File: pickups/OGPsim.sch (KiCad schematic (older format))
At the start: 6 parts, among them Q3 QSB363, Q4 QSB363

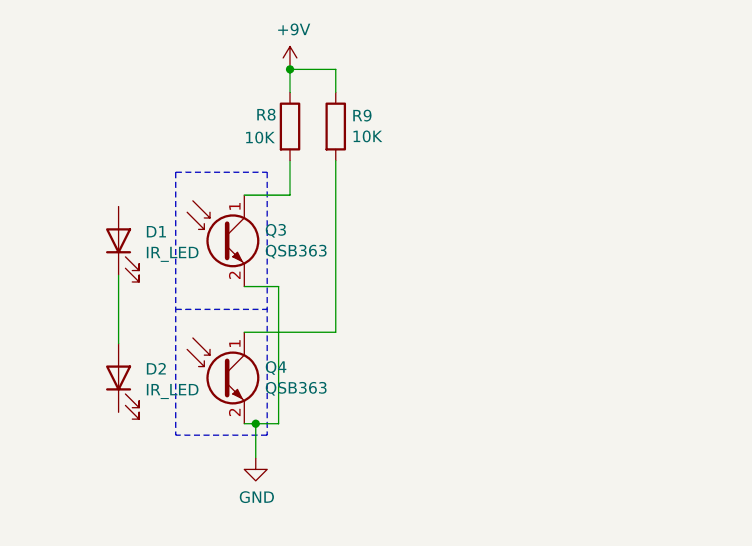
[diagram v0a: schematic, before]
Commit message: Added solder pads to pickup and adjusted placement of solder pads on demodulator.
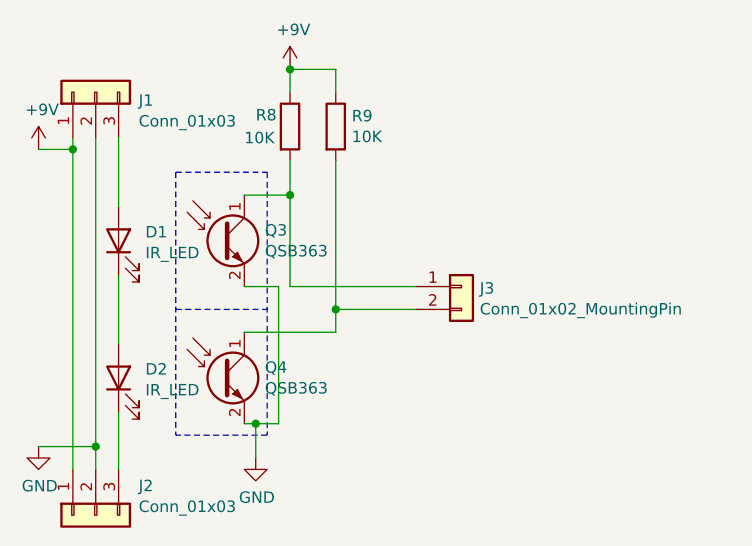
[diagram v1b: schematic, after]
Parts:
- added J1, J2: Conn_01x03, Connect:GS3, symbol Connector_Generic:Conn_01x03
- added J3: Conn_01x02_MountingPin, Connect:GS2, symbol Connector_Generic:Conn_01x02
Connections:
- net +9V: now also J1.1 (Pin_1), J2.1 (Pin_1)
- net GND: now also J1.2 (Pin_2), J2.2 (Pin_2)
- net at D1.2 (A): now also J1.3 (Pin_3)
- net at D2.1 (K): now also J2.3 (Pin_3)
- net at Q4.1 (C), R9.2: now also J3.2 (Pin_2)
- net at Q3.1 (C), R8.2: now also J3.1 (Pin_1)
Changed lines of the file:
@@
 	5150 4000 5550 4000
 Wire Wire Line
-	5850 3350 5850 4100
+	5850 3350 5850 4000
 $Comp
 L power:GND #PWR0102
@@
 Wire Wire Line
 	4900 3850 4900 4150
+$Comp
+L Connector_Generic:Conn_01x02 J3
+U 1 1 6127CF70
+P 6400 3900
+F 0 "J3" H 6480 3892 50  0000 L CNN
+F 1 "Conn_01x02_MountingPin" H 6480 3801 50  0000 L CNN
+F 2 "Connect:GS2" H 6400 3900 50  0001 C CNN
+F 3 "~" H 6400 3900 50  0001 C CNN
+	1    6400 3900
+	1    0    0    -1
+$EndComp
+Wire Wire Line
+	5850 4000 6200 4000
+Connection ~ 5850 4000
+Wire Wire Line
+	5850 4000 5850 4100
+Wire Wire Line
+	5650 3500 5650 3900
+Wire Wire Line
+	5650 3900 6200 3900
+Connection ~ 5650 3500
+$Comp
+L Connector_Generic:Conn_01x03 J1
+U 1 1 6127E563
+P 4800 3050
+F 0 "J1" V 4764 2862 50  0000 R CNN
+F 1 "Conn_01x03" V 4673 2862 50  0000 R CNN
+F 2 "Connect:GS3" H 4800 3050 50  0001 C CNN
+F 3 "~" H 4800 3050 50  0001 C CNN
+	1    4800 3050
+	0    -1   -1   0
+$EndComp
+$Comp
+L Connector_Generic:Conn_01x03 J2
+U 1 1 6127F19D
+P 4800 4900
+F 0 "J2" V 4672 4712 50  0000 R CNN
+F 1 "Conn_01x03" V 4763 4712 50  0000 R CNN
+F 2 "Connect:GS3" H 4800 4900 50  0001 C CNN
+F 3 "~" H 4800 4900 50  0001 C CNN
+	1    4800 4900
+	0    -1   1    0
+$EndComp
+Wire Wire Line
+	4900 3250 4900 3550
+Wire Wire Line
+	4900 4450 4900 4700
+$Comp
+L power:GND #PWR0101
+U 1 1 612806ED
+P 4550 4600
+F 0 "#PWR0101" H 4550 4350 50  0001 C CNN
+F 1 "GND" H 4555 4427 50  0000 C CNN
+F 2 "" H 4550 4600 50  0001 C CNN
+F 3 "" H 4550 4600 50  0001 C CNN
+	1    4550 4600
+	1    0    0    -1
+$EndComp
+$Comp
+L power:+9V #PWR0104
+U 1 1 612808C5
+P 4550 3300
+F 0 "#PWR0104" H 4550 3150 50  0001 C CNN
+F 1 "+9V" H 4565 3473 50  0000 C CNN
+F 2 "" H 4550 3300 50  0001 C CNN
+F 3 "" H 4550 3300 50  0001 C CNN
+	1    4550 3300
+	1    0    0    -1
+$EndComp
+Wire Wire Line
+	4800 4700 4800 4600
+Wire Wire Line
+	4550 3300 4700 3300
+Wire Wire Line
+	4700 3250 4700 3300
+Connection ~ 4700 3300
+Wire Wire Line
+	4700 3300 4700 4700
+Wire Wire Line
+	4550 4600 4800 4600
+Connection ~ 4800 4600
+Wire Wire Line
+	4800 4600 4800 3250
 $EndSCHEMATC
